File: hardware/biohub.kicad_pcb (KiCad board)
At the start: 2 copper layers, 55 x 55 mm, 20 parts, among them J1 1050170001, J2 Conn_02x13_Odd_Even, U1 ADUM1411BRWZ, U10 AD8244BRMZ, U11 AD8244BRMZ, U12 TPD4E1B06DCKR, U13 TPD4E1B06DCKR, U2 FT220XS, U3 ADUM6020, U4 ADP3605, U5 ADP7142AUJZ-2.5-R7, U6 ADP7182AUJZ-2.5-R7, U7 ADS1299IPAG, U8 AD8244BRMZ, U9 AD8244BRMZ

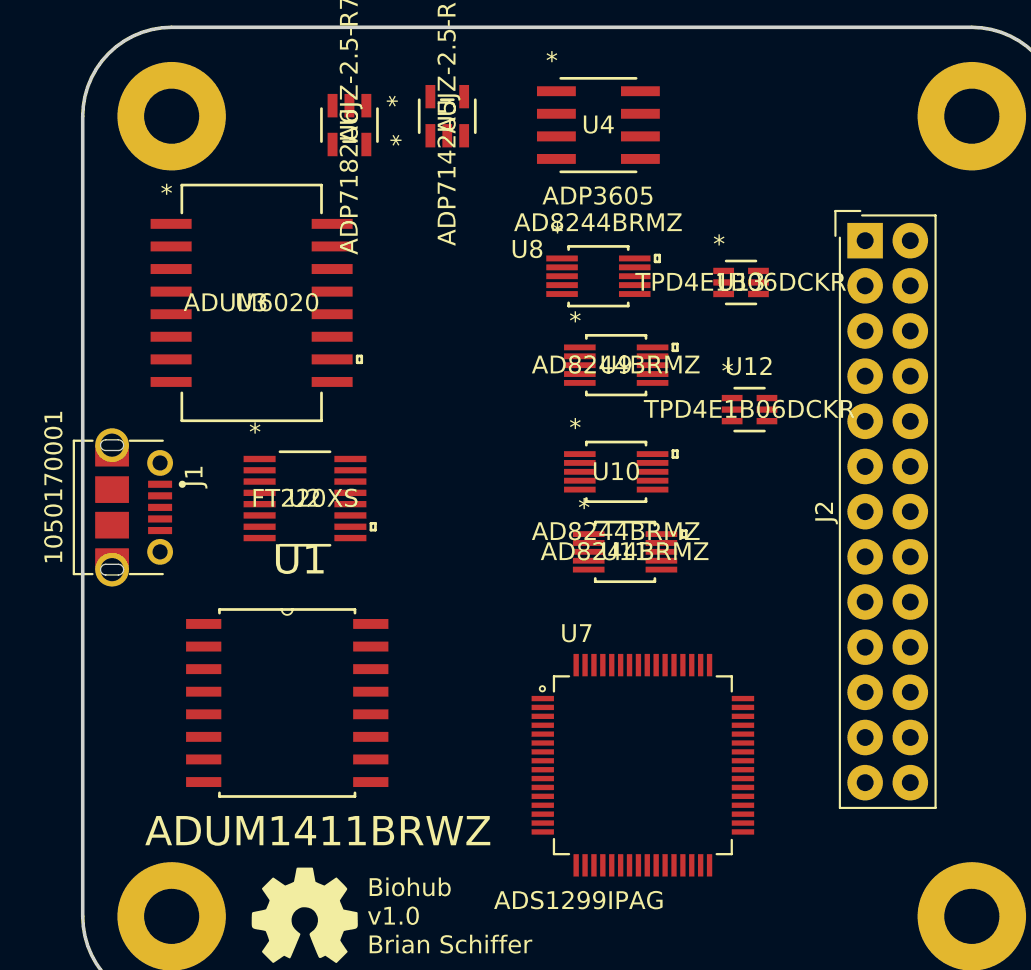
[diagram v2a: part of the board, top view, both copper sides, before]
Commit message: Part swaps & BOM completion
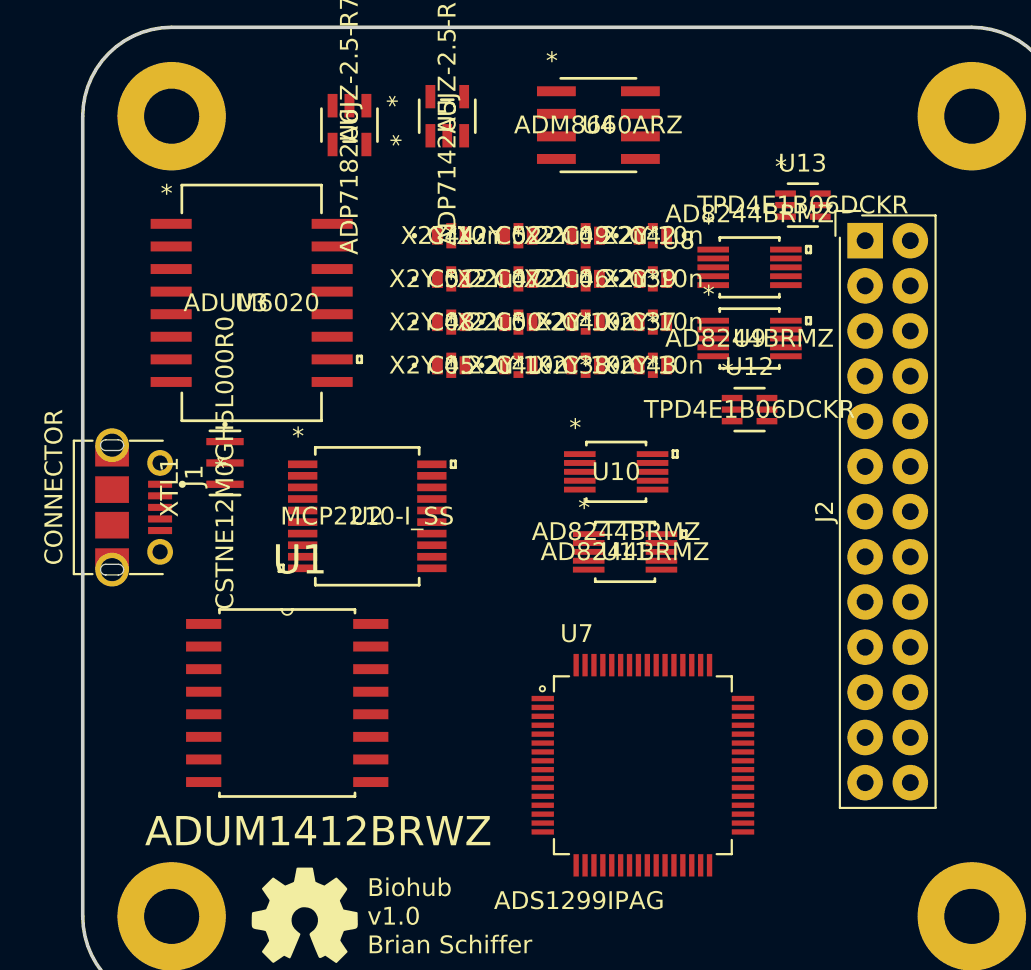
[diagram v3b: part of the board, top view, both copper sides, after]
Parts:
- added C37: X2Y 10n, biohub:500X14W103MV4T, F.Cu at (242.1, 96.6)
- added C38: X2Y 10n, biohub:500X14W103MV4T, F.Cu at (238.3, 99.0)
- added C39: X2Y 10n, biohub:500X14W103MV4T, F.Cu at (242.1, 94.1)
- added C40: X2Y 10n, biohub:500X14W103MV4T, F.Cu at (238.3, 96.6)
- added C41: X2Y 10n, biohub:500X14W103MV4T, F.Cu at (234.5, 99.0)
- added C42: X2Y 10n, biohub:500X14W103MV4T, F.Cu at (242.1, 91.7)
- added C43: X2Y 10n, biohub:500X14W103MV4T, F.Cu at (242.1, 99.0)
- added C44: X2Y 10n, biohub:500X14W103MV4T, F.Cu at (230.7, 91.7)
- added C45: X2Y 0.22u, biohub:160X14X224MV4T, F.Cu at (230.7, 99.0)
- added C46: X2Y 0.22u, biohub:160X14X224MV4T, F.Cu at (238.3, 94.1)
- added C47: X2Y 0.22u, biohub:160X14X224MV4T, F.Cu at (234.5, 94.1)
- added C48: X2Y 0.22u, biohub:160X14X224MV4T, F.Cu at (230.7, 96.6)
- added C49: X2Y 0.22u, biohub:160X14X224MV4T, F.Cu at (238.3, 91.7)
- added C50: X2Y 0.22u, biohub:160X14X224MV4T, F.Cu at (234.5, 96.6)
- added C51: X2Y 0.22u, biohub:160X14X224MV4T, F.Cu at (230.7, 94.1)
- added C52: X2Y 0.22u, biohub:160X14X224MV4T, F.Cu at (234.5, 91.7)
- added XTL1: CSTNE12M0GH5L000R0, biohub:CSTNE12M0GH5L000R0, F.Cu at (218.0, 104.5)
- J1: value 1050170001 -> CONNECTOR
- U1: value ADUM1411BRWZ -> ADUM1412BRWZ; footprint biohub:ADUM1411BRWZ -> biohub:ADUM1412BRWZ
- U2: value FT220XS -> MCP2210-I_SS; footprint biohub:FT220X -> biohub:MCP2210
- U4: value ADP3605 -> ADM8660ARZ; footprint biohub:ADP3605ARZ -> biohub:ADM8660ARZ
- moved U8 8.51 mm to (247.5, 93.5)
- moved U9 7.65 mm to (247.5, 97.5)
- moved U13 5.57 mm to (250.5, 90.0)
- moved U2 3.64 mm to (226.0, 107.5)
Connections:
- net /AFE/BIAS_INV renamed Net-(C20-Pad2)
- net /AFE/CS renamed Net-(R46-Pad2)
- net /interface/BIAS renamed /AFE/BIAS
- J2 pad 23: /interface/SRB2 -> /AFE/SRB2
- J2 pad 24: /interface/SRB1 -> /AFE/SRB1
- U1 pad 11: /usb/MISO -> /AFE/DRDY
- U1 pad 12: /usb/CS -> /AFE/MISO
- U1 pad 13: /usb/SCLK -> /AFE/MOSI
- U1 pad 14: /usb/MOSI -> GND
- U1 pad 3: /usb/USB_SPI_MOSI -> GNDD
- U1 pad 4: /usb/USB_SPI_CLK -> /usb/USB_SPI_MOSI
- U1 pad 5: /usb/USB_SPI_CS -> /usb/USB_SPI_MISO
- U1 pad 6: /usb/USB_SPI_MISO -> /usb/USB_SPI_DATA_READY
- U13 pad 2: /interface/SRB1 -> /AFE/SRB1
- U13 pad 4: /interface/SRB2 -> /AFE/SRB2
- U2 pad 1: /usb/USB_SPI_MOSI -> VBUS
- U2 pad 10: VCOM -> Net-(U2-Pad10)
- U2 pad 11: VCOM -> GNDD
- U2 pad 12: VBUS -> Net-(U2-Pad12)
- U2 pad 13: GNDD -> /usb/USB_SPI_MISO
- U2 pad 14: /usb/USB_SPI_CS -> /usb/USB_SPI_DATA_READY
- U2 pad 15: /usb/USB_SPI_CLK -> Net-(U2-Pad15)
- U2 pad 3: VCOM -> Net-(U2-Pad3)
- U2 pad 5: GNDD -> Net-(U2-Pad5)
- U2 pad 7: /usb/USB_SPI_MISO -> Net-(U2-Pad7)
- U2 pad 9: Net-(R2-Pad1) -> /usb/USB_SPI_MOSI
- U3 pad 11: GND -> Net-(C11-Pad2)
- U3 pad 13: GND -> Net-(C11-Pad2)
- U3 pad 14: GND -> Net-(C11-Pad2)
- U3 pad 15: GND -> Net-(C11-Pad2)
- U3 pad 9: GND -> Net-(C11-Pad2)
- U4 pad 1: Net-(C14-Pad1) -> GND
- U4 pad 2: GND -> Net-(C14-Pad1)
- U4 pad 3: Net-(C14-Pad2) -> GND
- U4 pad 4: GND -> Net-(C14-Pad2)
- U4 pad 5: Net-(R4-Pad2) -> -3V3
- U4 pad 6: Net-(U4-Pad6) -> GND
- U4 pad 7: -3V3 -> GND
- U7 pad 1: /AFE/IN8N -> /interface/8N
- U7 pad 10: /AFE/IN4P -> /interface/4P
- U7 pad 11: /AFE/IN3N -> /interface/3N
- U7 pad 12: /AFE/IN3P -> /interface/3P
- U7 pad 13: /AFE/IN2N -> /interface/2N
- U7 pad 14: /AFE/IN2P -> /interface/2P
- U7 pad 15: /AFE/IN1N -> /interface/1N
- U7 pad 16: /AFE/IN1P -> /interface/1P
- U7 pad 2: /AFE/IN8P -> /interface/8P
- U7 pad 3: /AFE/IN7N -> /interface/7N
- U7 pad 35: +3V3 -> Net-(R48-Pad2)
- U7 pad 4: /AFE/IN7P -> /interface/7P
- U7 pad 40: /AFE/SCLK -> GND
- U7 pad 47: Net-(U7-Pad47) -> /AFE/DRDY
- U7 pad 5: /AFE/IN6N -> /interface/6N
- U7 pad 6: /AFE/IN6P -> /interface/6P
- U7 pad 7: /AFE/IN5N -> /interface/5N
- U7 pad 8: /AFE/IN5P -> /interface/5P
- U7 pad 9: /AFE/IN4N -> /interface/4N

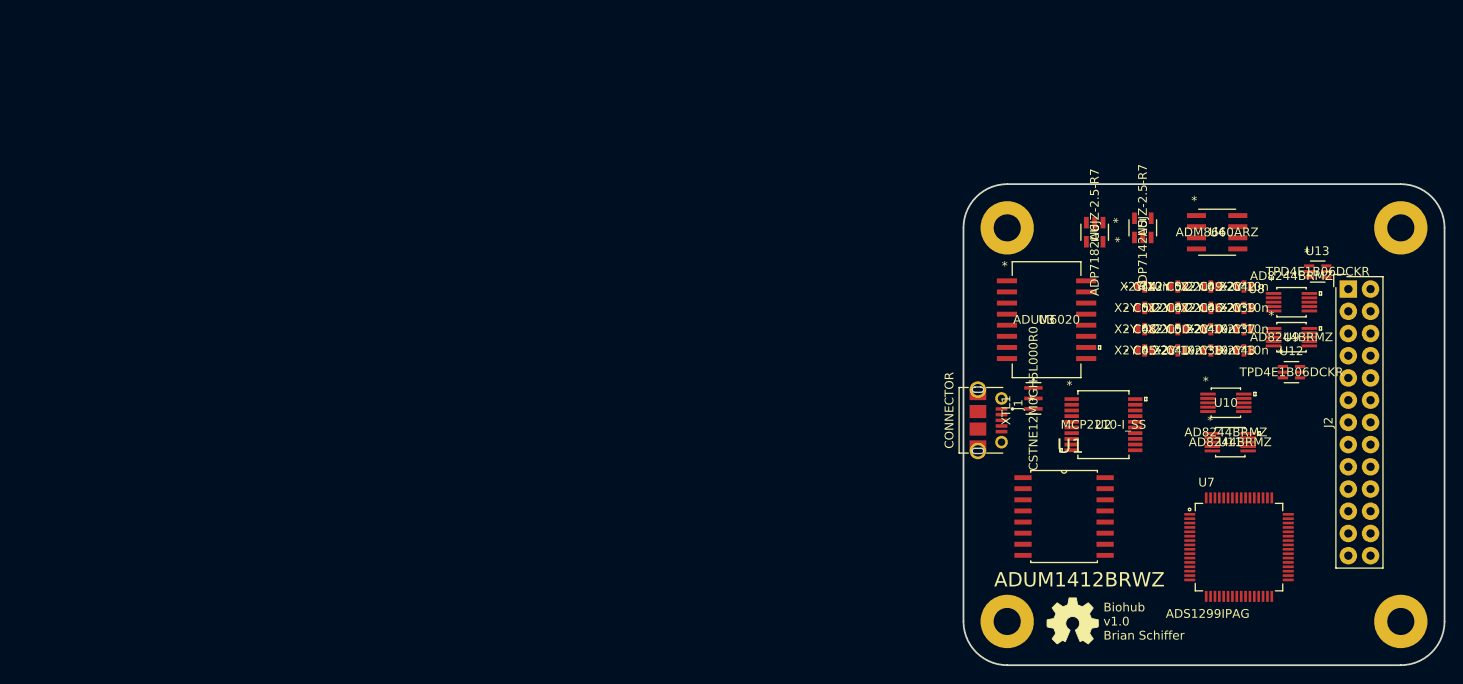
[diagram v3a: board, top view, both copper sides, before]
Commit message: Finished assigning footprints
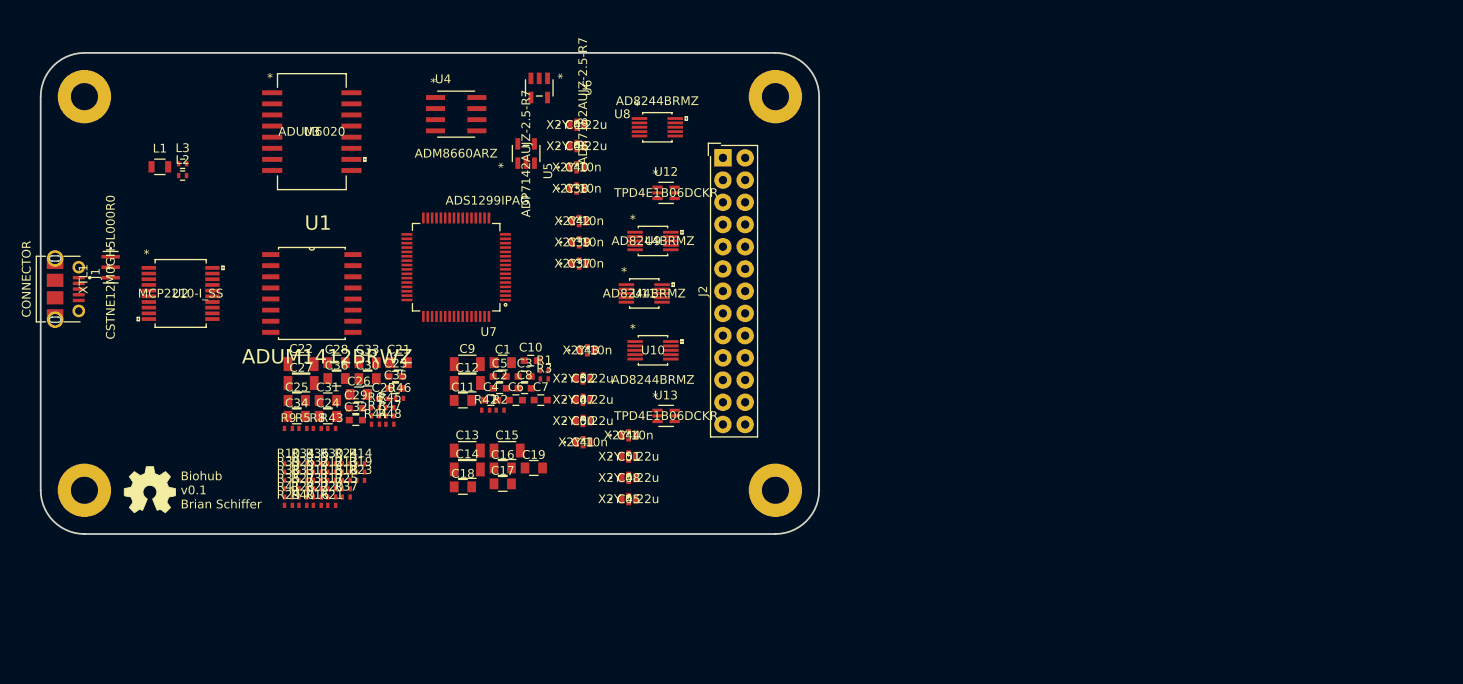
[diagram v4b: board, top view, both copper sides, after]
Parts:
- added C1: 4.7u, Capacitors_SMD:C_0805, F.Cu at (157.3, 100.4)
- added C10: 0.1u, Capacitors_SMD:C_0603, F.Cu at (160.5, 100.2)
- added C11: 0.22u, Capacitors_SMD:C_0805, F.Cu at (152.8, 104.7)
- added C12: 10u, Capacitors_SMD:C_1206, F.Cu at (153.3, 102.7)
- added C13: 10u, Capacitors_SMD:C_1206, F.Cu at (153.3, 110.5)
- added C14: 10u, Capacitors_SMD:C_1206, F.Cu at (153.3, 112.6)
- added C15: 10u, Capacitors_SMD:C_1206, F.Cu at (157.8, 110.5)
- added C16: 2.2u, Capacitors_SMD:C_0805, F.Cu at (157.3, 112.5)
- added C17: 2.2u, Capacitors_SMD:C_0805, F.Cu at (157.3, 114.3)
- added C18: 2.2u, Capacitors_SMD:C_0805, F.Cu at (152.8, 114.6)
- added C19: 2.2u, Capacitors_SMD:C_0805, F.Cu at (160.9, 112.5)
- added C2: 0.1u, Capacitors_SMD:C_0603, F.Cu at (157.0, 103.3)
- added C20: 1n, Capacitors_SMD:C_0402, F.Cu at (143.7, 104.6)
- added C21: 1u, Capacitors_SMD:C_0805, F.Cu at (145.4, 100.4)
- added C22: 10u, Capacitors_SMD:C_1206, F.Cu at (134.3, 100.6)
- added C23: 0.1u, Capacitors_SMD:C_0603, F.Cu at (145.1, 102.0)
- added C24: 1u, Capacitors_SMD:C_0805, F.Cu at (137.3, 106.6)
- added C25: 1u, Capacitors_SMD:C_0805, F.Cu at (133.8, 104.7)
- added C26: 1u, Capacitors_SMD:C_0805, F.Cu at (140.9, 104.1)
- added C27: 100u, Capacitors_SMD:C_1206, F.Cu at (134.3, 102.7)
- added C28: 1u, Capacitors_SMD:C_0805, F.Cu at (138.3, 100.4)
- added C29: 0.1u, Capacitors_SMD:C_0603, F.Cu at (140.5, 105.6)
- added C3: 10nF, Capacitors_SMD:C_0603, F.Cu at (159.8, 102.0)
- added C30: 1u, Capacitors_SMD:C_0805, F.Cu at (141.9, 102.2)
- added C31: 1u, Capacitors_SMD:C_0805, F.Cu at (137.3, 104.7)
- added C32: 0.1u, Capacitors_SMD:C_0603, F.Cu at (140.5, 107.0)
- added C33: 1u, Capacitors_SMD:C_0805, F.Cu at (141.9, 100.4)
- added C34: 1u, Capacitors_SMD:C_0805, F.Cu at (133.8, 106.6)
- added C35: 0.1u, Capacitors_SMD:C_0603, F.Cu at (145.1, 103.3)
- added C36: 1u, Capacitors_SMD:C_0805, F.Cu at (138.3, 102.2)
- added C4: 47p, Capacitors_SMD:C_0603, F.Cu at (156.0, 104.7)
- added C5: 0.1u, Capacitors_SMD:C_0603, F.Cu at (157.0, 102.0)
- added C6: 47p, Capacitors_SMD:C_0603, F.Cu at (158.8, 104.7)
- added C7: 0.1u, Capacitors_SMD:C_0603, F.Cu at (161.7, 104.7)
- added C8: 0.1u, Capacitors_SMD:C_0603, F.Cu at (159.8, 103.3)
- added C9: 10u, Capacitors_SMD:C_1206, F.Cu at (153.3, 100.6)
- added L1: 600R/2A, Inductors_SMD:L_0805, F.Cu at (118.1, 78.0)
- added L2: 2.2R/0.2A, Inductors_SMD:L_0402, F.Cu at (120.7, 79.0)
- added L3: 2.2R/0.2A, Inductors_SMD:L_0402, F.Cu at (120.7, 77.7)
- added R1: 10k, Resistors_SMD:R_0402_NoSilk, F.Cu at (162.1, 101.3)
- added R10: 4.02k 0.1%, Resistors_SMD:R_0402_NoSilk, F.Cu at (132.8, 112.0)
- added R11: 4.02k 0.1%, Resistors_SMD:R_0402_NoSilk, F.Cu at (136.1, 113.9)
- added R12: 4.02k 0.1%, Resistors_SMD:R_0402_NoSilk, F.Cu at (137.8, 112.9)
- added R13: 4.02k 0.1%, Resistors_SMD:R_0402_NoSilk, F.Cu at (139.4, 112.9)
- added R14: 4.02k 0.1%, Resistors_SMD:R_0402_NoSilk, F.Cu at (141.1, 112.0)
- added R15: 4.02k 0.1%, Resistors_SMD:R_0402_NoSilk, F.Cu at (137.8, 113.9)
- added R16: 4.02k 0.1%, Resistors_SMD:R_0402_NoSilk, F.Cu at (136.1, 116.7)
- added R17: 4.02k 0.1%, Resistors_SMD:R_0402_NoSilk, F.Cu at (137.8, 114.8)
- added R18: 4.02k 0.1%, Resistors_SMD:R_0402_NoSilk, F.Cu at (139.4, 113.9)
- added R19: 4.02k 0.1%, Resistors_SMD:R_0402_NoSilk, F.Cu at (141.1, 112.9)
- added R2: 27, Resistors_SMD:R_0402_NoSilk, F.Cu at (157.0, 105.8)
- added R20: 4.02k 0.1%, Resistors_SMD:R_0402_NoSilk, F.Cu at (137.8, 115.8)
- added R21: 4.02k 0.1%, Resistors_SMD:R_0402_NoSilk, F.Cu at (137.8, 116.7)
- added R22: 4.02k 0.1%, Resistors_SMD:R_0402_NoSilk, F.Cu at (136.1, 115.8)
- added R23: 4.02k 0.1%, Resistors_SMD:R_0402_NoSilk, F.Cu at (141.1, 113.9)
- added R24: 4.02k 0.1%, Resistors_SMD:R_0402_NoSilk, F.Cu at (139.4, 112.0)
- added R25: 4.02k 0.1%, Resistors_SMD:R_0402_NoSilk, F.Cu at (139.4, 114.8)
- added R26: 10k 0.1%, Resistors_SMD:R_0402_NoSilk, F.Cu at (134.5, 112.9)
- added R27: 10k 0.1%, Resistors_SMD:R_0402_NoSilk, F.Cu at (134.5, 114.8)
- added R28: 10k 0.1%, Resistors_SMD:R_0402_NoSilk, F.Cu at (134.5, 115.8)
- added R29: 10k 0.1%, Resistors_SMD:R_0402_NoSilk, F.Cu at (132.8, 116.7)
- added R3: 27, Resistors_SMD:R_0402_NoSilk, F.Cu at (162.1, 102.3)
- added R30: 10k 0.1%, Resistors_SMD:R_0402_NoSilk, F.Cu at (137.8, 112.0)
- added R31: 10k 0.1%, Resistors_SMD:R_0402_NoSilk, F.Cu at (136.1, 114.8)
- added R32: 10k 0.1%, Resistors_SMD:R_0402_NoSilk, F.Cu at (136.1, 112.9)
- added R33: 10k 0.1%, Resistors_SMD:R_0402_NoSilk, F.Cu at (134.5, 113.9)
- added R34: 10k 0.1%, Resistors_SMD:R_0402_NoSilk, F.Cu at (134.5, 112.0)
- added R35: 10k 0.1%, Resistors_SMD:R_0402_NoSilk, F.Cu at (132.8, 114.8)
- added R36: 10k 0.1%, Resistors_SMD:R_0402_NoSilk, F.Cu at (136.1, 112.0)
- added R37: 10k 0.1%, Resistors_SMD:R_0402_NoSilk, F.Cu at (139.4, 115.8)
- added R38: 10k 0.1%, Resistors_SMD:R_0402_NoSilk, F.Cu at (132.8, 113.9)
- added R39: 10k 0.1%, Resistors_SMD:R_0402_NoSilk, F.Cu at (132.8, 112.9)
- added R40: 10k 0.1%, Resistors_SMD:R_0402_NoSilk, F.Cu at (134.5, 116.7)
- added R41: 10k 0.1%, Resistors_SMD:R_0402_NoSilk, F.Cu at (132.8, 115.8)
- added R42: 10k, Resistors_SMD:R_0402_NoSilk, F.Cu at (155.4, 105.8)
- added R43: 10k, Resistors_SMD:R_0402_NoSilk, F.Cu at (137.8, 107.9)
- added R44: 10k, Resistors_SMD:R_0402_NoSilk, F.Cu at (142.8, 107.5)
- added R45: 1M, Resistors_SMD:R_0402_NoSilk, F.Cu at (144.4, 105.6)
- added R46: 10k, Resistors_SMD:R_0402_NoSilk, F.Cu at (145.5, 104.5)
- added R47: 10k, Resistors_SMD:R_0402_NoSilk, F.Cu at (144.4, 106.5)
- added R48: 10k, Resistors_SMD:R_0402_NoSilk, F.Cu at (144.4, 107.5)
- added R5: 1M, Resistors_SMD:R_0402_NoSilk, F.Cu at (134.5, 107.9)
- added R6: 10k, Resistors_SMD:R_0402_NoSilk, F.Cu at (142.8, 105.6)
- added R7: 10k, Resistors_SMD:R_0402_NoSilk, F.Cu at (142.8, 106.5)
- added R8: 10k, Resistors_SMD:R_0402_NoSilk, F.Cu at (136.1, 107.9)
- added R9: 10k, Resistors_SMD:R_0402_NoSilk, F.Cu at (132.8, 107.9)
- moved ? 106.6 mm to (111.2, 72.2)
- moved ? 106.6 mm to (117.0, 115.0)
- moved J1 106.6 mm to (106.5, 92.0)
- moved U2 106.6 mm to (120.5, 92.5)
- moved XTL1 106.6 mm to (112.5, 89.5)
- moved ? 106.6 mm to (110.1, 115.3)
- moved U7 95.0 mm to (152.0, 89.5), turned to 180 degrees
- moved U1 89.7 mm to (135.5, 92.5)
- moved U4 88.0 mm to (152.0, 72.0)
- moved U3 86.7 mm to (135.5, 74.0)
- moved C37 76.4 mm to (166.1, 89.1)
- moved C39 76.4 mm to (166.1, 86.6)
- moved C42 76.4 mm to (166.1, 84.2)
- moved U13 76.3 mm to (176.0, 106.5)
- moved U8 75.2 mm to (175.0, 73.5)
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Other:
- board size 55 x 55 mm -> 89 x 55 mm
- copper layers 2 -> 4
- board text added: "Biohub v0.1 Brian Schiffer"
- board text removed: "2"
- board text removed: "3"
- board text removed: "Biohub v1.0 Brian Schiffer"
